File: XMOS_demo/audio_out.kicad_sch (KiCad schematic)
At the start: 38 parts, among them J5 Conn_01x06_Socket, J6 Conn_01x06_Socket, J7 AudioJack3_SwitchT, U7 MAX97220C

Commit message: routing
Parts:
- added H5: M3_NPTH, MountingHole:MountingHole_3.2mm_M3, symbol Mechanical:MountingHole
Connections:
- net GND: now also J5.1 (Pin_1); no longer J5.6 (Pin_6)
- net INR+: now also J6.3 (Pin_3); no longer J6.2 (Pin_2)
- net INR-: now also J6.2 (Pin_2); no longer J6.3 (Pin_3)
- net OUT_A+: now also J5.3 (Pin_3); no longer J5.2 (Pin_2)
- net OUT_A-: now also J5.2 (Pin_2); no longer J5.3 (Pin_3)
- net P5V0: now also J5.6 (Pin_6); no longer J5.1 (Pin_1)
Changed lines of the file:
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@@
 	(wire
 		(pts
-			(xy 45.72 22.86) (xy 45.72 25.4)
+			(xy 38.1 30.48) (xy 38.1 25.4)
 		)
 		(stroke
@@
 	(wire
 		(pts
-			(xy 45.72 40.64) (xy 45.72 38.1)
+			(xy 30.48 33.02) (xy 30.48 38.1)
 		)
 		(stroke
@@
 	(wire
 		(pts
-			(xy 45.72 38.1) (xy 53.34 38.1)
+			(xy 30.48 38.1) (xy 53.34 38.1)
 		)
 		(stroke
@@
 	(wire
 		(pts
-			(xy 45.72 25.4) (xy 53.34 25.4)
+			(xy 38.1 25.4) (xy 53.34 25.4)
 		)
 		(stroke
@@
 		)
 	)
-	(label "OUT_A+"
+	(label "OUT_A-"
 		(at 43.18 27.94 0)
 		(effects
@@
 		)
 	)
+	(label "INR+"
+		(at 121.92 30.48 180)
+		(effects
+			(font
+				(size 1.27 1.27)
+			)
+			(justify right bottom)
+		)
+	)
 	(label "R_INL-"
 		(at 162.56 76.2 180)
@@
 		)
 	)
-	(label "INR-"
-		(at 121.92 30.48 180)
-		(effects
-			(font
-				(size 1.27 1.27)
-			)
-			(justify right bottom)
-		)
-	)
 	(label "OUT_B-"
 		(at 66.04 129.54 180)
@@
 		)
 	)
-	(label "AMP_OUTR"
-		(at 228.6 83.82 0)
+	(label "INR-"
+		(at 121.92 27.94 180)
 		(effects
 			(font
 				(size 1.27 1.27)
 			)
-			(justify left bottom)
+			(justify right bottom)
 		)
 	)
-	(label "INR+"
-		(at 121.92 27.94 180)
+	(label "AMP_OUTR"
+		(at 228.6 83.82 0)
 		(effects
 			(font
 				(size 1.27 1.27)
 			)
-			(justify right bottom)
+			(justify left bottom)
 		)
 	)
@@
 		)
 	)
-	(label "OUT_A-"
-		(at 43.18 30.48 0)
-		(effects
-			(font
-				(size 1.27 1.27)
-			)
-			(justify left bottom)
-		)
-	)
 	(label "INL+"
 		(at 121.92 33.02 180)
@@
 		)
 	)
+	(label "OUT_A+"
+		(at 43.18 30.48 0)
+		(effects
+			(font
+				(size 1.27 1.27)
+			)
+			(justify left bottom)
+		)
+	)
 	(label "INR-"
 		(at 111.76 71.12 0)
@@
 	)
 	(symbol
+		(lib_id "Mechanical:MountingHole")
+		(at 82.55 27.94 0)
+		(unit 1)
+		(exclude_from_sim no)
+		(in_bom no)
+		(on_board yes)
+		(dnp no)
+		(fields_autoplaced yes)
+		(property "Reference" "H5"
+			(at 85.09 26.6699 0)
+			(effects
+				(font
+					(size 1.27 1.27)
+				)
+				(justify left)
+			)
+		)
+		(property "Value" "M3_NPTH"
+			(at 85.09 29.2099 0)
+			(effects
+				(font
+					(size 1.27 1.27)
+				)
+				(justify left)
+			)
+		)
+		(property "Footprint" "MountingHole:MountingHole_3.2mm_M3"
+			(at 82.55 27.94 0)
+			(effects
+				(font
+					(size 1.27 1.27)
+				)
+				(hide yes)
+			)
+		)
+		(property "Datasheet" "~"
+			(at 82.55 27.94 0)
+			(effects
+				(font
+					(size 1.27 1.27)
+				)
+				(hide yes)
+			)
+		)
+		(property "Description" "Mounting Hole without connection"
+			(at 82.55 27.94 0)
+			(effects
+				(font
+					(size 1.27 1.27)
+				)
+				(hide yes)
+			)
+		)
+		(instances
+			(project "XMOS_demo"
+				(path "/0a855fb0-ca19-4770-811e-70d8770d7fdd/82ce7187-f0cb-4a8a-9f6c-b1803f49d1ca"
+					(reference "H5")
+					(unit 1)
+				)
+			)
+		)
+	)
+	(symbol
 		(lib_id "Device:R_Small")
 		(at 167.64 93.98 90)
@@
 	(symbol
 		(lib_id "power:GND")
-		(at 45.72 40.64 0)
+		(at 38.1 30.48 0)
 		(unit 1)
 		(exclude_from_sim no)
@@
 		(dnp no)
 		(property "Reference" "#PWR062"
-			(at 45.72 46.99 0)
+			(at 38.1 36.83 0)
 			(effects
 				(font
@@
 		)
 		(property "Value" "GND"
-			(at 45.72 44.45 0)
+			(at 38.1 34.29 0)
 			(effects
 				(font
@@
 		)
 		(property "Footprint" ""
-			(at 45.72 40.64 0)
+			(at 38.1 30.48 0)
 			(effects
 				(font
@@
 		)
 		(property "Datasheet" ""
-			(at 45.72 40.64 0)
+			(at 38.1 30.48 0)
 			(effects
 				(font
@@
 		)
 		(property "Description" "Power symbol creates a global label with name \"GND\" , ground"
-			(at 45.72 40.64 0)
+			(at 38.1 30.48 0)
 			(effects
 				(font
@@
 	(symbol
 		(lib_id "_power:P5V0")
-		(at 45.72 22.86 0)
+		(at 30.48 33.02 0)
 		(unit 1)
 		(exclude_from_sim no)
@@
 		(dnp no)
 		(property "Reference" "#PWR060"
-			(at 45.72 26.67 0)
+			(at 30.48 36.83 0)
 			(effects
 				(font
@@
 		)
 		(property "Value" "P5V0"
-			(at 45.72 19.304 0)
+			(at 30.48 29.464 0)
 			(effects
 				(font
@@
 		)
 		(property "Footprint" ""
-			(at 45.72 22.86 0)
+			(at 30.48 33.02 0)
 			(effects
 				(font
@@
 		)
 		(property "Datasheet" ""
-			(at 45.72 22.86 0)
+			(at 30.48 33.02 0)
 			(effects
 				(font
@@
 		)
 		(property "Description" "Power symbol creates a global label with name \"P5V0\""
-			(at 45.72 22.86 0)
+			(at 30.48 33.02 0)
 			(effects
 				(font

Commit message: sch and pcb changes - output filter
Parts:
- added C48, C50, C54, C56: 470n, Capacitor_SMD:C_1206_3216Metric_Pad1.33x1.80mm_HandSolder, symbol Device:C_Small
- renumbered C46 to C41, C49 to C42, C53 to C43, C57 to C44, C59 to C45, C60 to C46, C41 to C47, C47 to C49, C50 to C51, C45 to C53, C48 to C55, C51 to C57, C54 to C58, C42 to C59, C43 to C60, C44 to C87, C56 to C88, C58 to C89, C55 to C90, R32 to R31, R34 to R32, R41 to R33, R42 to R34, R37 to R36, R33 to R37, R36 to R38, R31 to R39, R39 to R41, R38 to R42, U7 to U2
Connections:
- net INL+: now also C50.1
- net INL-: now also C56.1
- net INR+: now also C48.1
- net INR-: now also C54.1
- net R_INL+: now also C50.2
- net R_INL-: now also C56.2
- net R_INR+: now also C48.2
- net R_INR-: now also C54.2
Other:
- moved on the sheet: C47, C49, C53, C55, H5, J5, J6

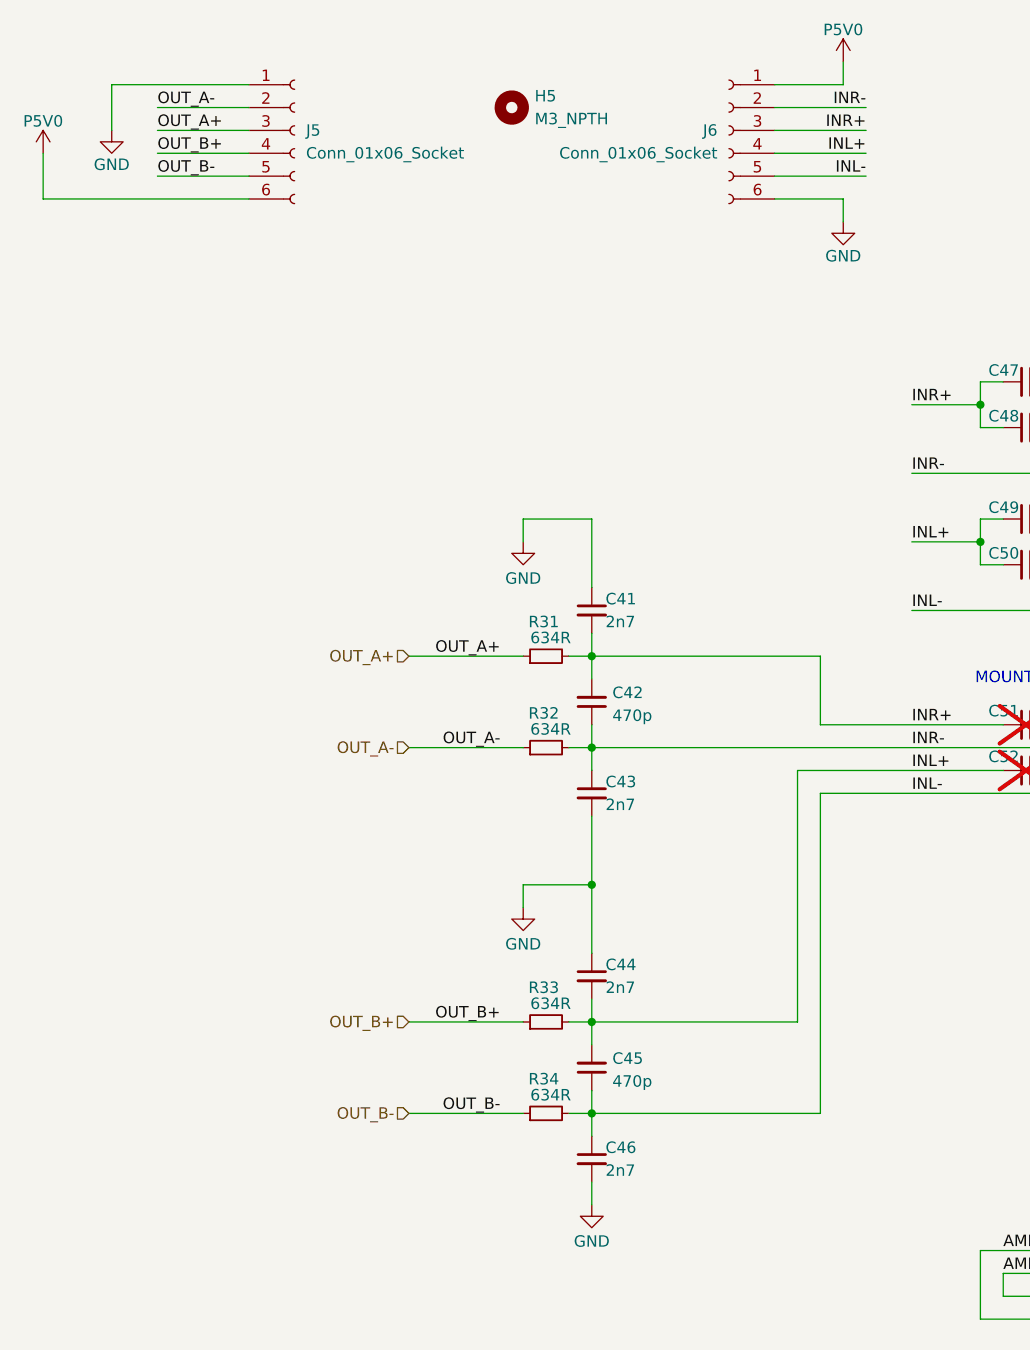
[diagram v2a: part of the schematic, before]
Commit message: added schematic and simulation for active output filter
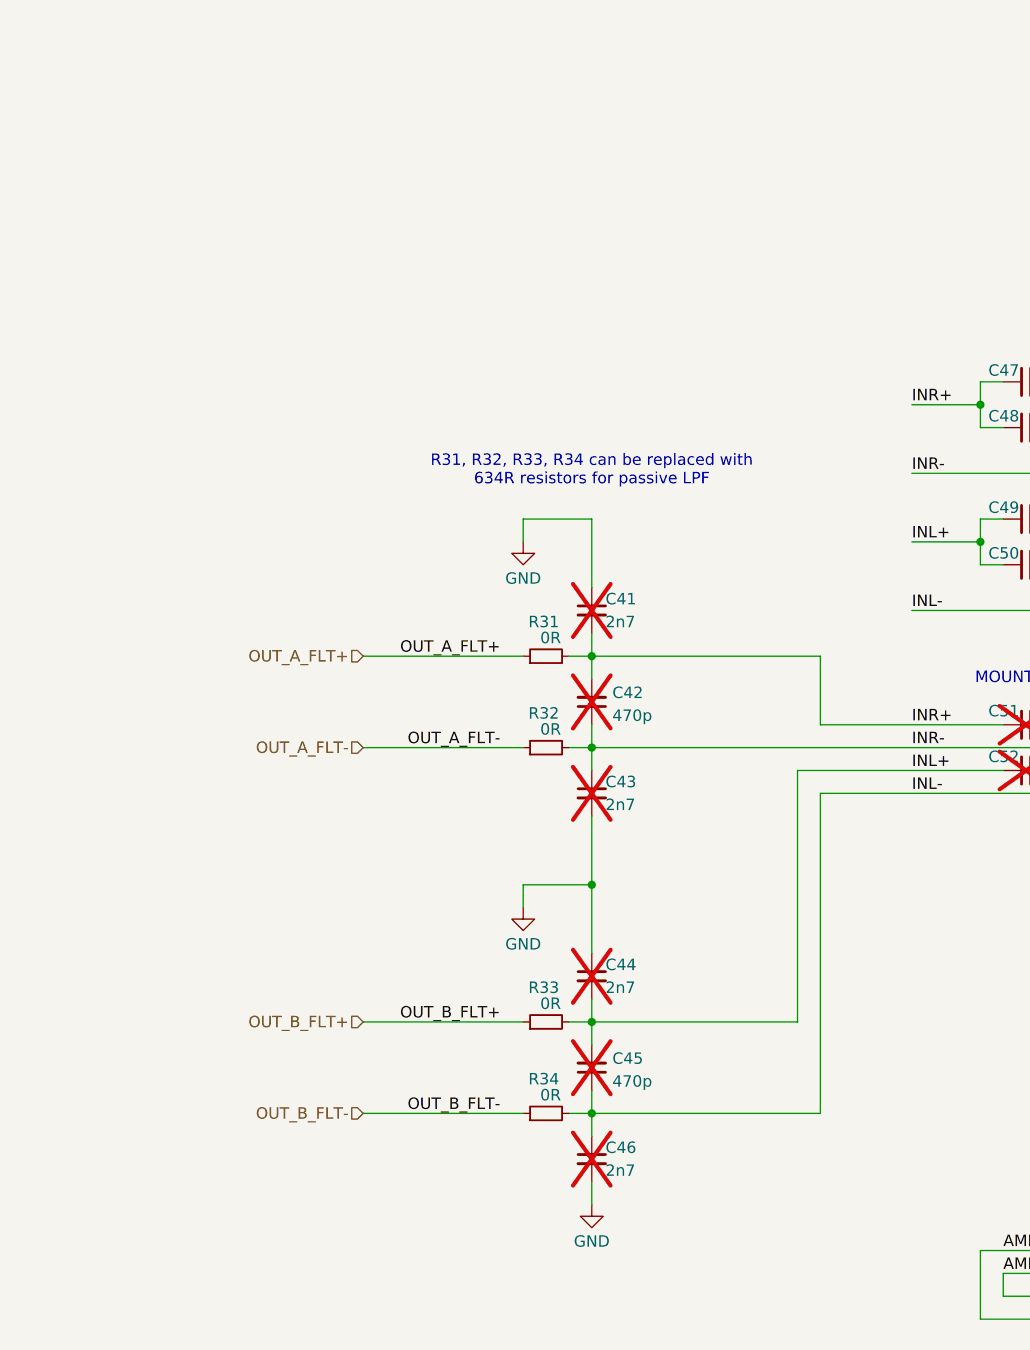
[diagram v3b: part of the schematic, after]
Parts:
- removed H5: M3_NPTH, MountingHole:MountingHole_3.2mm_M3, symbol Mechanical:MountingHole
- removed J5, J6: Conn_01x06_Socket, Connector_PinHeader_2.54mm:PinHeader_1x06_P2.54mm_Vertical, symbol Connector:Conn_01x06_Socket
- C41, C42, C43, C44, C45, C46: now not fitted
- R31: value 634R -> 0R; footprint Resistor_SMD:R_0603_1608Metric -> Resistor_SMD:R_0603_1608Metri
- R32, R33, R34: value 634R -> 0R
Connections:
- net OUT_A+ renamed OUT_A_FLT+
- net OUT_A- renamed OUT_A_FLT-
- net OUT_B+ renamed OUT_B_FLT+
- net OUT_B- renamed OUT_B_FLT-
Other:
- note added: "R31, R32, R33, R34 can be replaced with 634R resistors for passive LPF"

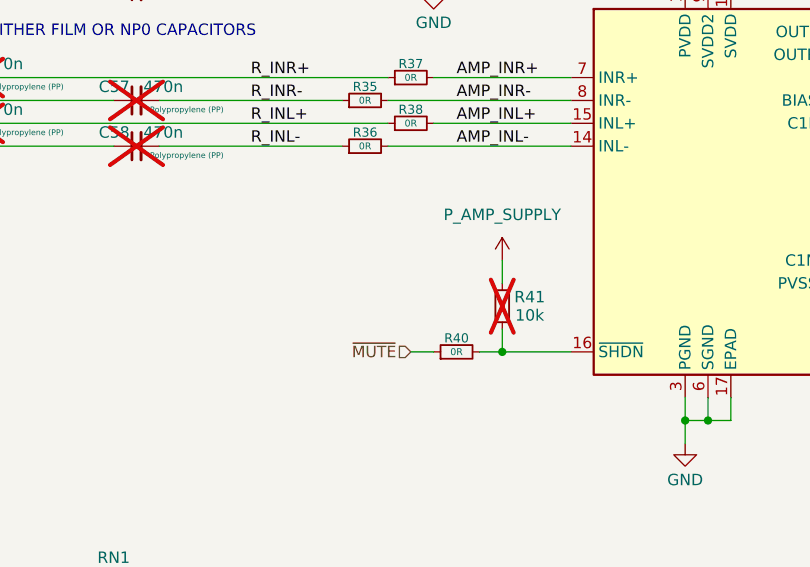
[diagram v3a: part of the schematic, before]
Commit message: Updated sch and pcb with active filter
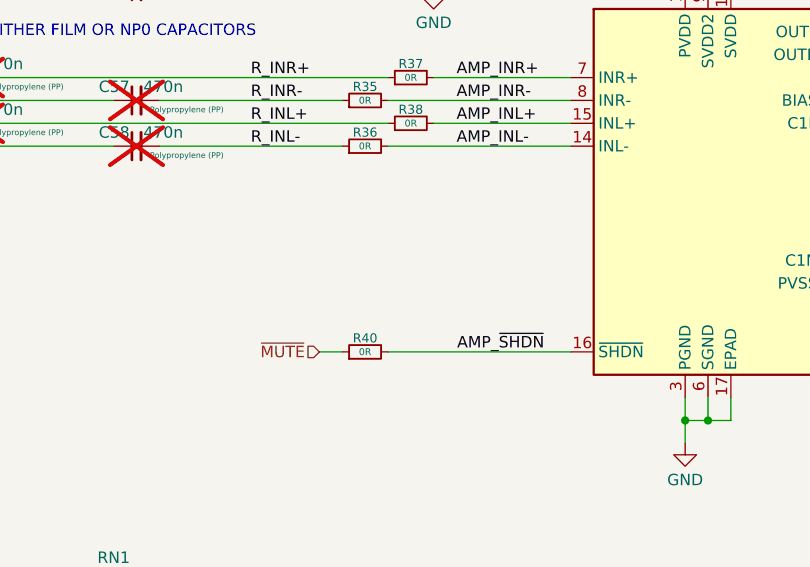
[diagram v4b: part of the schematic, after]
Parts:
- removed R41: 10k, Resistor_SMD:R_0603_1608Metric, symbol Device:R_Small
- R31: footprint Resistor_SMD:R_0603_1608Metri -> Resistor_SMD:R_0603_1608Metric
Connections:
- net AMP_~{SHDN}: now reaches R40.2, U2.16 (~{SHDN})
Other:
- moved on the sheet: R40
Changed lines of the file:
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@@
 	)
 	(junction
-		(at 182.88 116.84)
-		(diameter 0)
-		(color 0 0 0 0)
-	)
-	(junction
 		(at 185.42 63.5)
 		(diameter 0)
@@
 	(wire
 		(pts
-			(xy 172.72 116.84) (xy 175.26 116.84)
+			(xy 162.56 116.84) (xy 165.1 116.84)
 		)
 		(stroke
@@
 	(wire
 		(pts
-			(xy 182.88 114.3) (xy 182.88 116.84)
-		)
-		(stroke
-			(width 0)
-			(type default)
-		)
-	)
-	(wire
-		(pts
 			(xy 144.78 144.78) (xy 157.48 144.78)
 		)
@@
 	(wire
 		(pts
-			(xy 182.88 106.68) (xy 182.88 109.22)
-		)
-		(stroke
-			(width 0)
-			(type default)
-		)
-	)
-	(wire
-		(pts
 			(xy 127 86.36) (xy 170.18 86.36)
 		)
@@
 	(wire
 		(pts
-			(xy 180.34 116.84) (xy 182.88 116.84)
-		)
-		(stroke
-			(width 0)
-			(type default)
-		)
-	)
-	(wire
-		(pts
 			(xy 119.38 66.04) (xy 119.38 68.58)
 		)
@@
 	(wire
 		(pts
-			(xy 182.88 116.84) (xy 190.5 116.84)
+			(xy 170.18 116.84) (xy 190.5 116.84)
 		)
 		(stroke
@@
 		)
 	)
+	(label "AMP_~{SHDN}"
+		(at 177.8641 116.84 0)
+		(effects
+			(font
+				(size 1.27 1.27)
+			)
+			(justify left bottom)
+		)
+	)
 	(label "OUT_B_FLT-"
 		(at 66.04 129.54 180)
@@
 	(hierarchical_label "~{MUTE}"
 		(shape input)
-		(at 172.72 116.84 180)
+		(at 162.56 116.84 180)
 		(effects
 			(font
@@
 	(symbol
 		(lib_id "Device:R_Small")
-		(at 177.8 116.84 90)
+		(at 167.64 116.84 90)
 		(unit 1)
 		(exclude_from_sim no)
@@
 		(dnp no)
 		(property "Reference" "R40"
-			(at 177.8 115.316 90)
+			(at 167.64 115.316 90)
 			(effects
 				(font
@@
 		)
 		(property "Value" "0R"
-			(at 177.8 116.84 90)
+			(at 167.64 116.84 90)
 			(effects
 				(font
@@
 		)
 		(property "Footprint" "Resistor_SMD:R_0603_1608Metric"
-			(at 177.8 116.84 0)
+			(at 167.64 116.84 0)
 			(effects
 				(font
@@
 		)
 		(property "Datasheet" "~"
-			(at 177.8 116.84 0)
+			(at 167.64 116.84 0)
 			(effects
 				(font
@@
 		)
 		(property "Description" "Resistor, small symbol"
-			(at 177.8 116.84 0)
+			(at 167.64 116.84 0)
 			(effects
 				(font
@@
 	)
 	(symbol
+		(lib_id "Device:R_Small")
+		(at 71.12 78.74 90)
+		(unit 1)
+		(exclude_from_sim no)
+		(in_bom yes)
+		(on_board yes)
+		(dnp no)
+		(property "Reference" "R31"
+			(at 70.866 74.93 90)
+			(effects
+				(font
+					(size 1.27 1.27)
+				)
+			)
+		)
+		(property "Value" "0R"
+			(at 71.628 76.708 90)
+			(effects
+				(font
+					(size 1.27 1.27)
+				)
+			)
+		)
+		(property "Footprint" "Resistor_SMD:R_0603_1608Metric"
+			(at 71.12 78.74 0)
+			(effects
+				(font
+					(size 1.27 1.27)
+				)
+				(hide yes)
+			)
+		)
+		(property "Datasheet" "~"
+			(at 71.12 78.74 0)
+			(effects
+				(font
+					(size 1.27 1.27)
+				)
+				(hide yes)
+			)
+		)
+		(property "Description" "Resistor, small symbol"
+			(at 71.12 78.74 0)
+			(effects
+				(font
+					(size 1.27 1.27)
+				)
+				(hide yes)
+			)
+		)
+		(pin "1"
+		)
+		(pin "2"
+		)
+		(instances
+			(project "XMOS_demo"
+				(path "/0a855fb0-ca19-4770-811e-70d8770d7fdd/82ce7187-f0cb-4a8a-9f6c-b1803f49d1ca"
+					(reference "R31")
+					(unit 1)
+				)
+			)
+		)
+	)
+	(symbol
 		(lib_id "Device:R_Pack04")
 		(at 139.7 149.86 270)
@@
 	)
 	(symbol
-		(lib_id "_power:P_AMP_SUPPLY")
-		(at 182.88 106.68 0)
-		(unit 1)
-		(exclude_from_sim no)
-		(in_bom yes)
-		(on_board yes)
-		(dnp no)
-		(fields_autoplaced yes)
-		(property "Reference" "#PWR070"
-			(at 182.88 110.49 0)
-			(effects
-				(font
-					(size 1.27 1.27)
-				)
-				(hide yes)
-			)
-		)
-		(property "Value" "P_AMP_SUPPLY"
-			(at 182.88 101.6 0)
-			(effects
-				(font
-					(size 1.27 1.27)
-				)
-			)
-		)
-		(property "Footprint" ""
-			(at 182.88 106.68 0)
-			(effects
-				(font
-					(size 1.27 1.27)
-				)
-				(hide yes)
-			)
-		)
-		(property "Datasheet" ""
-			(at 182.88 106.68 0)
-			(effects
-				(font
-					(size 1.27 1.27)
-				)
-				(hide yes)
-			)
-		)
-		(property "Description" "Power symbol creates a global label with name \"P_AMP_SUPPLY\""
-			(at 182.88 106.68 0)
-			(effects
-				(font
-					(size 1.27 1.27)
-				)
-				(hide yes)
-			)
-		)
-		(pin "1"
-		)
-		(instances
-			(project "XMOS_demo"
-				(path "/0a855fb0-ca19-4770-811e-70d8770d7fdd/82ce7187-f0cb-4a8a-9f6c-b1803f49d1ca"
-					(reference "#PWR070")
-					(unit 1)
-				)
-			)
-		)
-	)
-	(symbol
 		(lib_id "Device:C_Small")
 		(at 226.06 99.06 0)
@@
 					(unit 1)
 				)
-			)
-		)
-	)
-	(symbol
-		(lib_id "Device:R_Small")
-		(at 182.88 111.76 0)
-		(unit 1)
-		(exclude_from_sim no)
-		(in_bom yes)
-		(on_board yes)
-		(dnp yes)
-		(property "Reference" "R41"
-			(at 185.928 110.744 0)
-			(effects
-				(font
-					(size 1.27 1.27)
-				)
-			)
-		)
-		(property "Value" "10k"
-			(at 185.928 112.776 0)
-			(effects
-				(font
-					(size 1.27 1.27)
-				)
-			)
-		)
-		(property "Footprint" "Resistor_SMD:R_0603_1608Metric"
-			(at 182.88 111.76 0)
-			(effects
-				(font
-					(size 1.27 1.27)
-				)
-				(hide yes)
-			)
-		)
-		(property "Datasheet" "~"
-			(at 182.88 111.76 0)
-			(effects
-				(font
-					(size 1.27 1.27)
-				)
-				(hide yes)
-			)
-		)
-		(property "Description" "Resistor, small symbol"
-			(at 182.88 111.76 0)
-			(effects
-				(font
-					(size 1.27 1.27)
-				)
-				(hide yes)
-			)
-		)
-		(pin "1"
-		)
-		(pin "2"
-		)
-		(instances
-			(project "XMOS_demo"
-				(path "/0a855fb0-ca19-4770-811e-70d8770d7fdd/82ce7187-f0cb-4a8a-9f6c-b1803f49d1ca"
-					(reference "R41")
-					(unit 1)
-				)
-			)
-		)
-	)
-	(symbol
-		(lib_id "Device:R_Small")
-		(at 71.12 78.74 90)
-		(unit 1)
-		(exclude_from_sim no)
-		(in_bom yes)
-		(on_board yes)
-		(dnp no)
-		(property "Reference" "R31"
-			(at 70.866 74.93 90)
-			(effects
-				(font
-					(size 1.27 1.27)
-				)
-			)
-		)
-		(property "Value" "0R"
-			(at 71.628 76.708 90)
-			(effects
-				(font
-					(size 1.27 1.27)
-				)
-			)
-		)
-		(property "Footprint" "Resistor_SMD:R_0603_1608Metri"
-			(at 71.12 78.74 0)
-			(effects
-				(font
-					(size 1.27 1.27)
-				)
-				(hide yes)
-			)
-		)
-		(property "Datasheet" "~"
-			(at 71.12 78.74 0)
-			(effects
-				(font
-					(size 1.27 1.27)
-				)
-				(hide yes)
-			)
-		)
-		(property "Description" "Resistor, small symbol"
-			(at 71.12 78.74 0)
-			(effects
-				(font
-					(size 1.27 1.27)
-				)
-				(hide yes)
-			)
-		)
-		(pin "1"
-		)
-		(pin "2"
-		)
-		(instances
-			(project "XMOS_demo"
-				(path "/0a855fb0-ca19-4770-811e-70d8770d7fdd/82ce7187-f0cb-4a8a-9f6c-b1803f49d1ca"
-					(reference "R31")
-					(unit 1)
-				)
